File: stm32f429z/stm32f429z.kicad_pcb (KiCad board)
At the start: 4 copper layers, 153 x 114.3 mm, 76 parts, among them J1 ADC connector 2, J10 UART 1 connectors, J11 CAN connector, J12 USB to UART GPIO, J13 USB_OTG, J14 I2C 1 connector, J2 ADC connector 1, J3 SPI 2 connector, J4 SPI 1 connector, J5 I2C 2 connector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

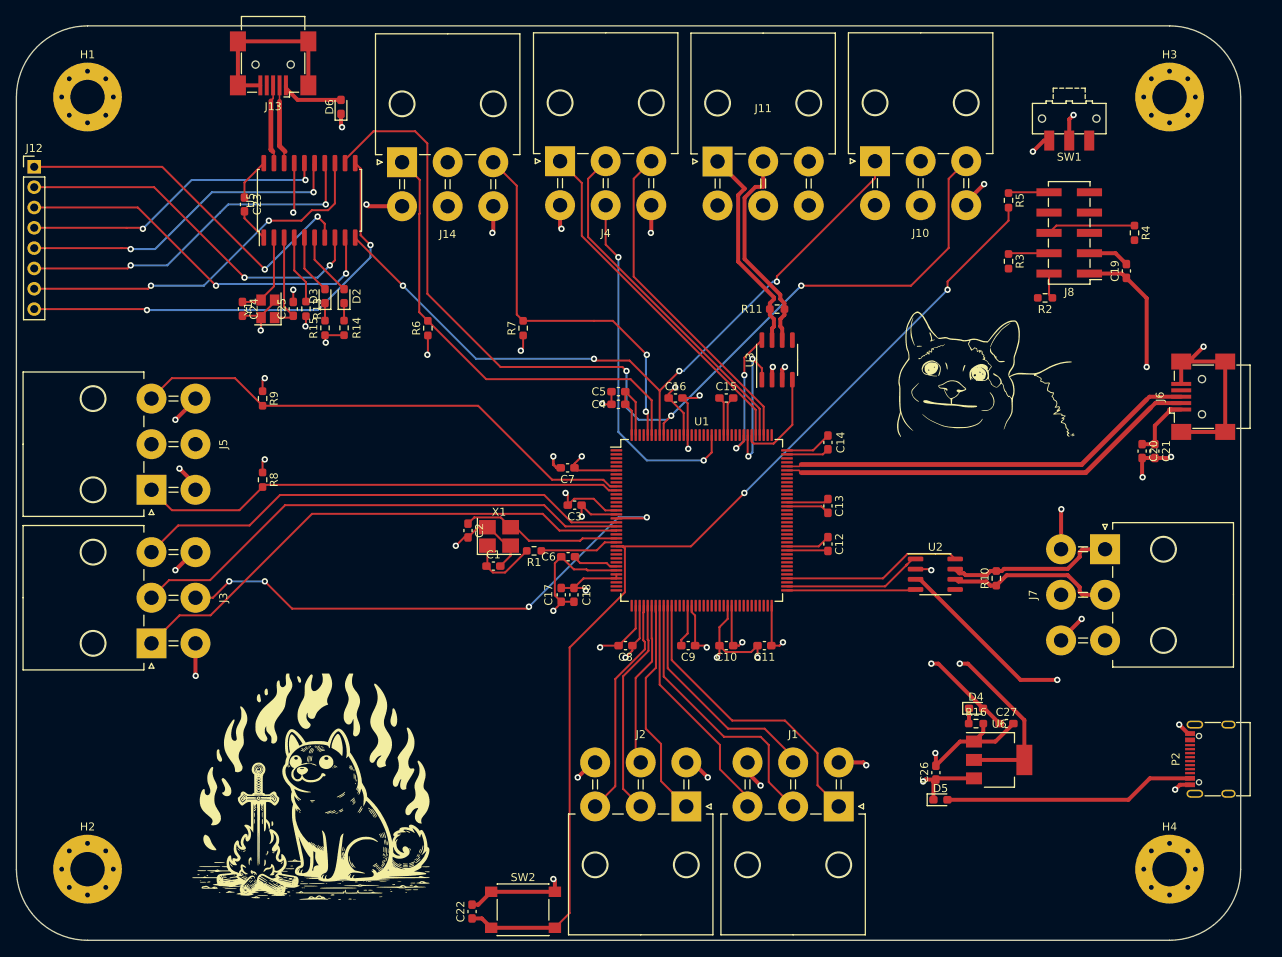
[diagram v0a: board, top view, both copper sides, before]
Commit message: removed alot of the silk screen, changed oscillator foor print and added GPIOs
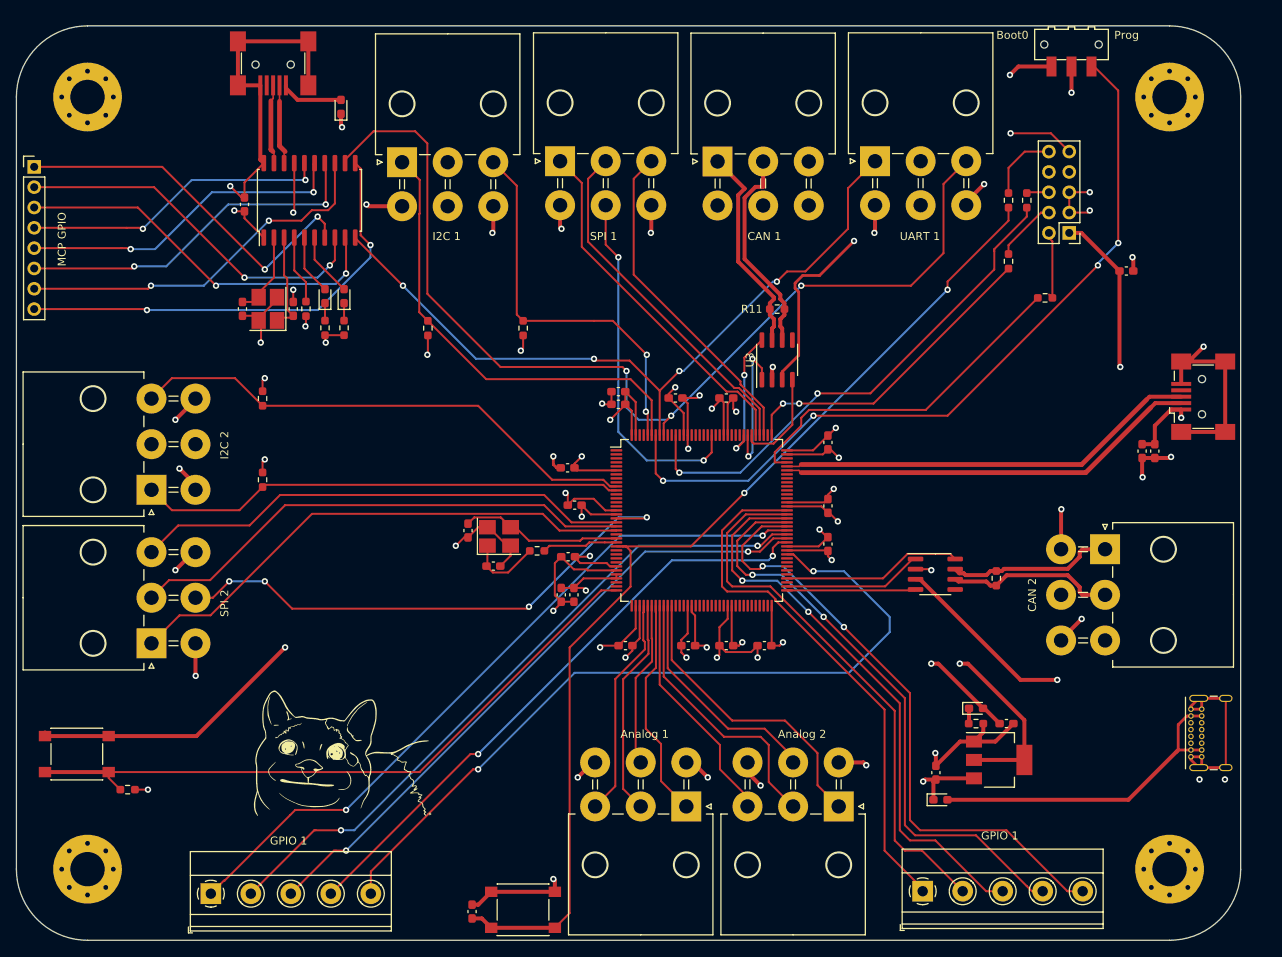
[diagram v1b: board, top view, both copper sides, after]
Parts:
- removed the G*** at (104.6, 132.6)
- added J15: GPIO, TerminalBlock_Phoenix:TerminalBlock_Phoenix_MKDS-1,5-5_1x05_P5.00mm_Horizontal, F.Cu at (181.3, 144.8)
- added J16: GPIO, TerminalBlock_Phoenix:TerminalBlock_Phoenix_MKDS-1,5-5_1x05_P5.00mm_Horizontal, F.Cu at (92.3, 145.1)
- added R12: 2k2, Resistor_SMD:R_0603_1608Metric_Pad0.98x0.95mm_HandSolder, F.Cu at (81.9, 132.1)
- added SW4: Logging BTN, Button_Switch_SMD:SW_SPST_PTS645, F.Cu at (75.6, 127.6)
- J8: footprint Connector_PinHeader_2.54mm:PinHeader_2x05_P2.54mm_Vertical_SMD -> Connector_PinHeader_2.54mm:PinHeader_2x05_P2.54mm_Vertical
- P2: footprint Connector_USB:USB_C_Receptacle_G-Switch_GT-USB-7010ASV -> Connector_USB:USB_C_Receptacle_GCT_USB4085
- Y1: footprint Crystal:Crystal_SMD_3225-4Pin_3.2x2.5mm -> Crystal:Crystal_SMD_3225-4Pin_3.2x2.5mm_HandSoldering
- moved G*** 93.3 mm to (108.6, 127.6)
- moved R4 14.1 mm to (194.3, 58.4)
- moved SW1 9.27 mm to (199.9, 38.9)
- moved P2 3.63 mm to (214.8, 128.0)
- moved R1 0.38 mm to (133.1, 102.2)
- turned C19 to 0 degrees
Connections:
- U1 pad 36: unconnected-(U1-PA2-Pad36) -> logging
- U1 pad 82: unconnected-(U1-PD13-Pad82) -> MCU_GPIO10
- U1 pad 85: unconnected-(U1-PD14-Pad85) -> MCU_GPIO9
- U1 pad 86: unconnected-(U1-PD15-Pad86) -> MCU_GPIO8
- U1 pad 87: unconnected-(U1-PG2-Pad87) -> MCU_GPIO7
- U1 pad 88: unconnected-(U1-PG3-Pad88) -> MCU_GPIO6
- U1 pad 89: unconnected-(U1-PG4-Pad89) -> MCU_GPIO5
- U1 pad 90: unconnected-(U1-PG5-Pad90) -> MCU_GPIO4
- U1 pad 91: unconnected-(U1-PG6-Pad91) -> MCU_GPIO3
- U1 pad 92: unconnected-(U1-PG7-Pad92) -> MCU_GPIO2
- U1 pad 93: unconnected-(U1-PG8-Pad93) -> MCU_GPIO1
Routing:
- net BOOT0: track 0.43 -> 99.1 mm, vias 0 -> 4
- net MCU_GPIO10: track 0.00 -> 98.0 mm, vias 0 -> 2
- net MCU_GPIO6: track 0.00 -> 90.8 mm, vias 0 -> 2
- net MCU_GPIO7: track 0.00 -> 85.6 mm, vias 0 -> 2
- net logging: track 0.00 -> 84.1 mm
- net MCU_GPIO8: track 0.00 -> 80.4 mm, vias 0 -> 2
- net MCU_GPIO5: track 0.00 -> 77.9 mm, vias 0 -> 2
- net MCU_GPIO9: track 0.00 -> 75.8 mm, vias 0 -> 2
- net MCU_GPIO4: track 0.00 -> 74.7 mm, vias 0 -> 2
- net MCU_GPIO3: track 0.00 -> 71.8 mm, vias 0 -> 2
- net MCU_GPIO2: track 0.00 -> 69.5 mm
- net MCU_GPIO1: track 0.00 -> 68.6 mm
- net SYS_JTDO-SWO: track 0.00 -> 64.3 mm, vias 0 -> 2
- net GND: track 244.9 -> 305.6 mm, vias 31 -> 42
- net +3.3V: track 153.2 -> 200.5 mm, vias 17 -> 25
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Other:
- board text added: "Analog 1"
- board text added: "Analog 2"
- board text added: "Boot0"
- board text added: "CAN 1"
- board text added: "CAN 2"
- board text added: "GPIO 1"
- board text added: "I2C 1"
- board text added: "I2C 2"
- board text added: "MCP GPIO"
- board text added: "Prog"
- board text added: "SPI 1"
- board text added: "SPI 2"
- board text added: "UART 1"

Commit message: changed logging schematic, tweaked some parts of the schematic
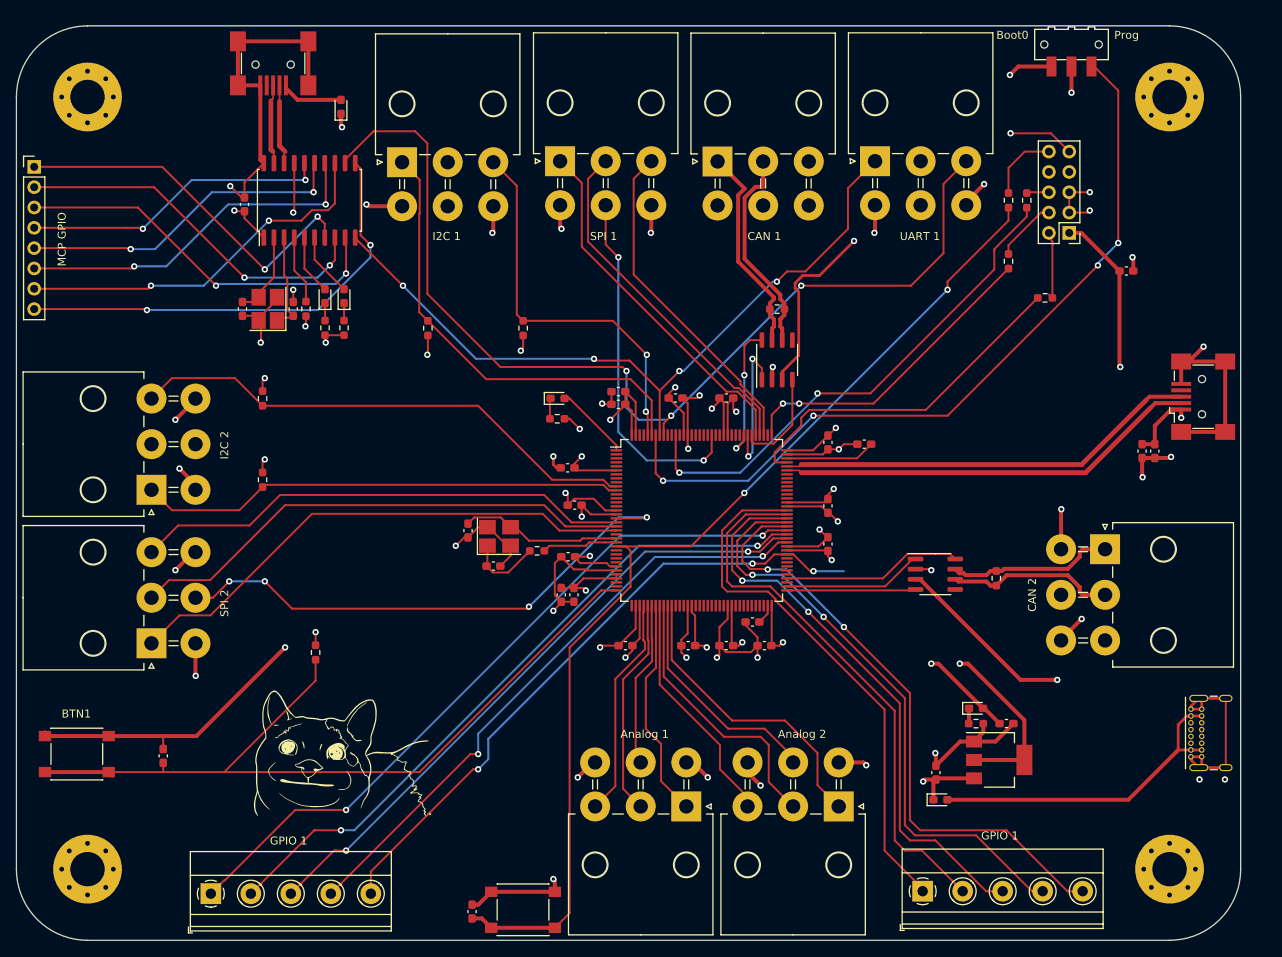
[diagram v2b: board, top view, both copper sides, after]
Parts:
- added C28: C, Capacitor_SMD:C_0603_1608Metric_Pad1.08x0.95mm_HandSolder, F.Cu at (86.4, 127.9)
- added C29: 22u, Capacitor_SMD:C_0603_1608Metric_Pad1.08x0.95mm_HandSolder, F.Cu at (174.0, 88.9)
- added C30: 22u, Capacitor_SMD:C_0603_1608Metric_Pad1.08x0.95mm_HandSolder, F.Cu at (160.0, 111.1)
- added D1: LED, LED_SMD:LED_0603_1608Metric_Pad1.05x0.95mm_HandSolder, F.Cu at (135.7, 83.2)
- added R17: 2k2, Resistor_SMD:R_0603_1608Metric_Pad0.98x0.95mm_HandSolder, F.Cu at (135.6, 85.7)
- C27: value 10u -> 22u
- moved R12 29.1 mm to (105.4, 114.9), turned to -90 degrees
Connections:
- R12 pad 1: logging -> +3.3V
- R12 pad 2: GND -> logging
- SW4 pad 1: +3.3V -> GND
- U1 pad 1: unconnected-(U1-PE2-Pad1) -> Net-(D1-A)
- U1 pad 106: unconnected-(U1-VCAP_2-Pad106) -> Net-(U1-VCAP_2)
- U1 pad 71: unconnected-(U1-VCAP_1-Pad71) -> Net-(U1-VCAP_1)
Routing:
- net GND: track 305.6 -> 349.0 mm, vias 42 -> 43
- net +3.3V: track 200.5 -> 166.8 mm
- net logging: track 84.1 -> 101.9 mm
- net MCU_GPIO10: track 98.0 -> 80.7 mm, vias 2 -> 3
- net Net-(U1-VCAP_2): track 0.00 -> 11.3 mm
- net Net-(D1-A): track 0.00 -> 9.54 mm
- net Net-(D1-K): track 0.00 -> 2.58 mm
- net Net-(U1-VCAP_1): track 0.00 -> 2.47 mm
- net MCU_GPIO9: track 75.8 -> 76.7 mm
- net CAN SIlent Mode 1: track 16.9 -> 17.8 mm
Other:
- board text added: "BTN1"

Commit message: changed some footprints, removed dimensions( was causing issues), addd a gerber filter for manufacturing(probably should be regenerated), added a BOM list
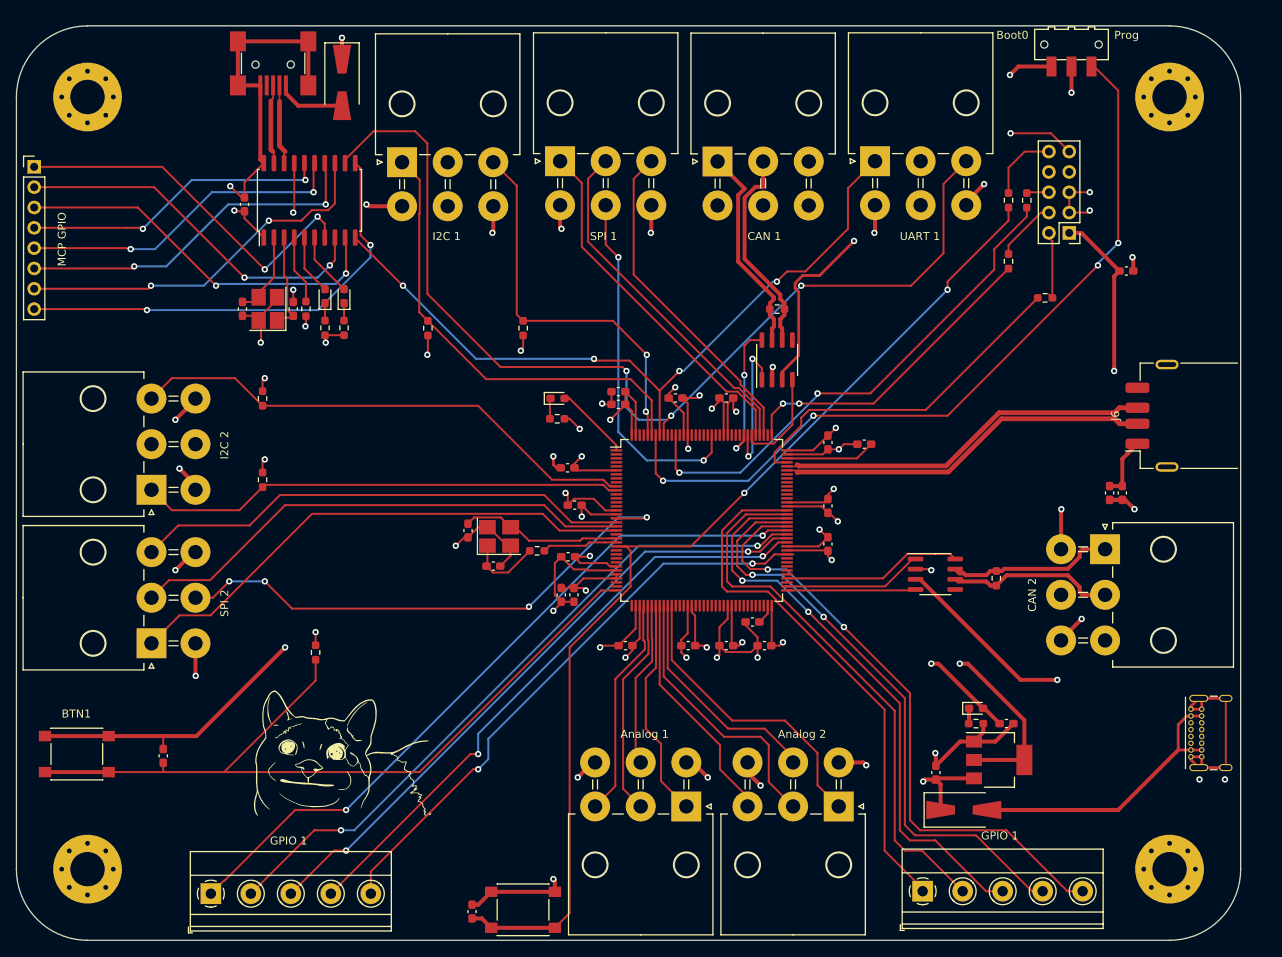
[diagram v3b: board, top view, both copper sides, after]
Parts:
- C28: value C -> 100n
- D5, D6: footprint Diode_SMD:D_0603_1608Metric_Pad1.05x0.95mm_HandSolder -> Diode_SMD:D_SMA-SMB_Universal_Handsoldering
- J6: footprint Connector_USB:USB_Mini-B_Wuerth_65100516121_Horizontal -> Connector_USB:USB_A_Receptacle_GCT_USB1046
- R12: value 2k2 -> 10k
- moved C21 6.63 mm to (206.2, 95.0)
- moved C20 6.63 mm to (204.7, 95.0)
- moved D5 3.19 mm to (186.4, 134.6)
- moved D6 3.05 mm to (108.7, 43.7), turned to -90 degrees
- moved J6 2.51 mm to (215.4, 85.3)
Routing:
- net GND: track 349.0 -> 322.0 mm, vias 43 -> 41
- net MCU_GPIO10: track 80.7 -> 73.5 mm, vias 3 -> 2
- net USB_OTG_FS_DP-: track 53.0 -> 47.0 mm
- net USB_OTG_FS_DP+: track 52.9 -> 47.0 mm
- net Net-(D5-A): track 40.9 -> 36.5 mm
- net +5V: track 116.5 -> 118.7 mm, vias 14 -> 13
- net Net-(D6-A): track 7.84 -> 8.65 mm

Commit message: added a folder for custom footprints and added more vias on the 5V and the gnd planes
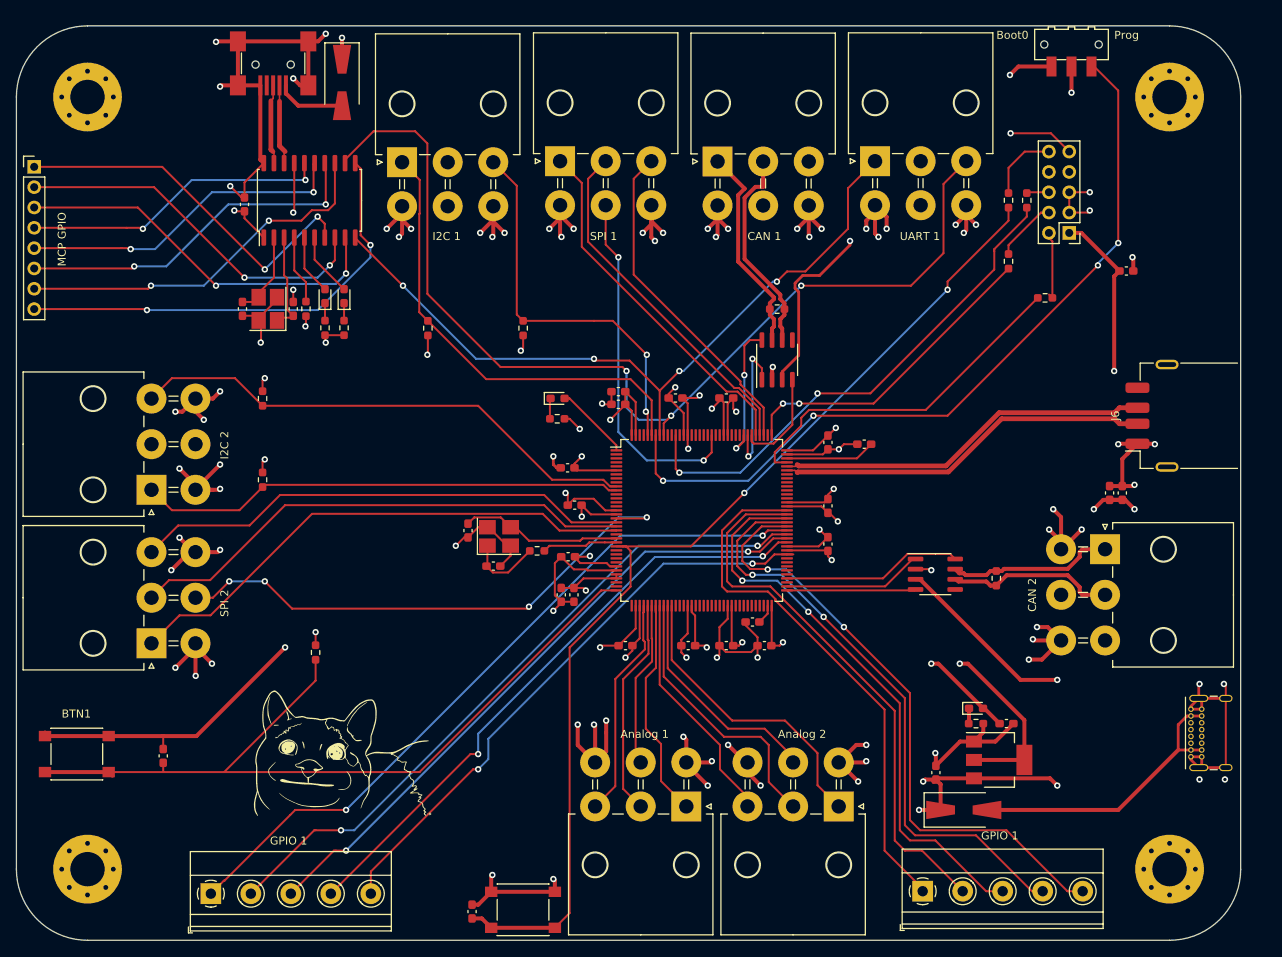
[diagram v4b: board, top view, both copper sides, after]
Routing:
- net +5V: track 118.7 -> 213.7 mm, vias 13 -> 37
- net GND: track 322.0 -> 415.4 mm, vias 41 -> 67

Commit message: usb footprint changes, Silkscreen markers for pin 1 in ICs and polarity for other components. Edited excel BOM list and kicad list for BOM cost.
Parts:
- J6: footprint Connector_USB:USB_A_Receptacle_GCT_USB1046 -> Connector_USB:USB_A_Molex_67643_Horizontal
- moved J6 5.58 mm to (211.0, 88.8)
- moved D5 3.56 mm to (190.0, 134.6)
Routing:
- net GND: track 415.4 -> 433.2 mm, vias 67 -> 73
- net +5V: track 213.7 -> 217.9 mm, vias 37 -> 36
- net Net-(D5-A): track 36.5 -> 32.9 mm
- net USB_OTG_FS_DP-: track 47.0 -> 49.9 mm
- net USB_OTG_FS_DP+: track 47.0 -> 49.9 mm
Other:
- board text added: "1/19 V1"
- board text added: "SWD"
- board text added: "USB"

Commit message: finished the CAN IMU schematic and pcb. Only needs some final touhces and a BOM list
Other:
- board text added: "PWR"
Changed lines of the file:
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@@
+    (effects (font (size 1 1) (thickness 0.15)) (justify left bottom))
+  )
+  (gr_text "Prog\n" (at 98.425 48.26) (layer "F.SilkS")
     (effects (font (size 1 1) (thickness 0.15)) (justify left bottom))
   )
@@
     (effects (font (size 1 1) (thickness 0.15)) (justify left bottom))
   )
+  (gr_text "PWR\n" (at 212.09 123.825 -90) (layer "F.SilkS")
+    (effects (font (size 1 1) (thickness 0.15)) (justify left bottom))
+  )

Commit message: added logo to the back silkscreen
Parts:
- added G***: LOGO, LOGO, B.Cu at (143.5, 92.6)
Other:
- board text added: "1/19/24 REV 1"
- board text removed: "1/19 V1"
